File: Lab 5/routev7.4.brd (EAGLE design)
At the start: 100 x 80 mm, 48 parts, among them J2 FTDI_DEVICE, M1 WIRELESS-NRF24L01, U2 GY-521MPU6050, U3 ATMEGA328P_TQFP

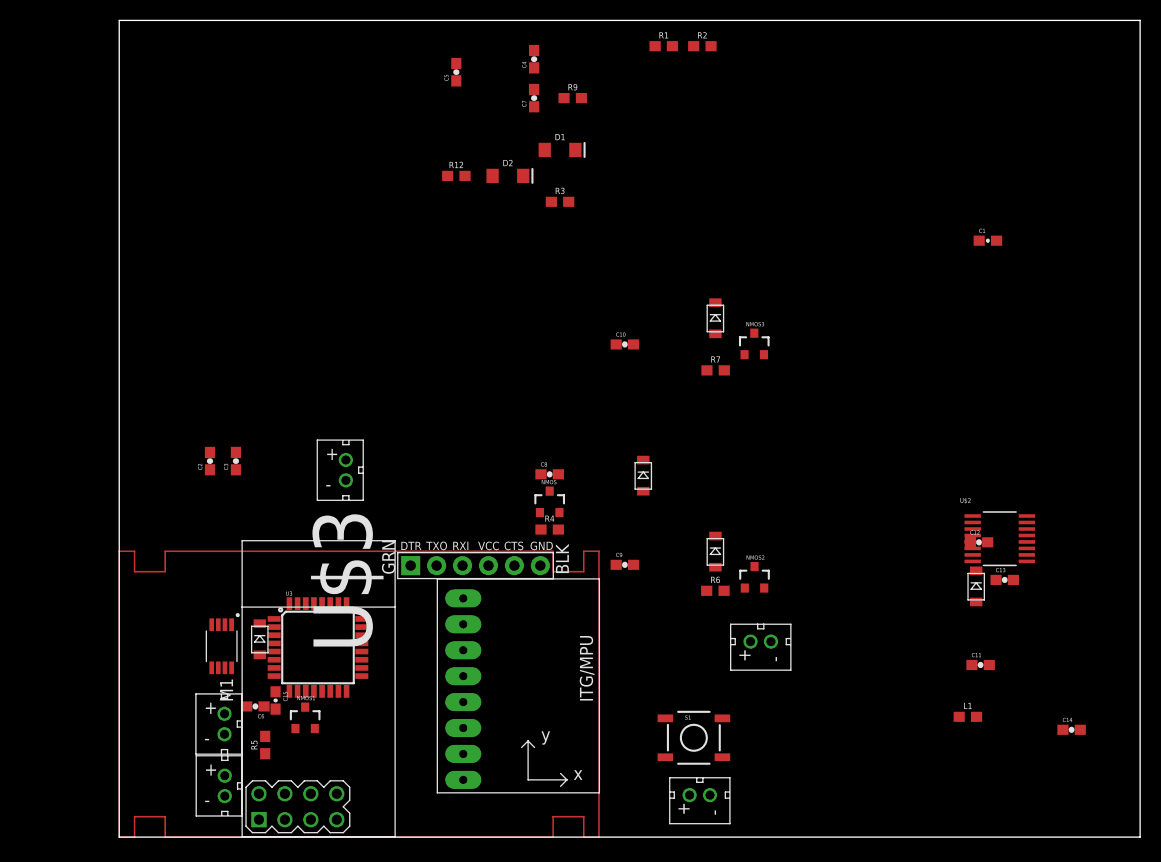
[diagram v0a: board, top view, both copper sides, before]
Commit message: Latest PCB at routev7.4.brd: no DRC error!!! Hurray!!!!!!
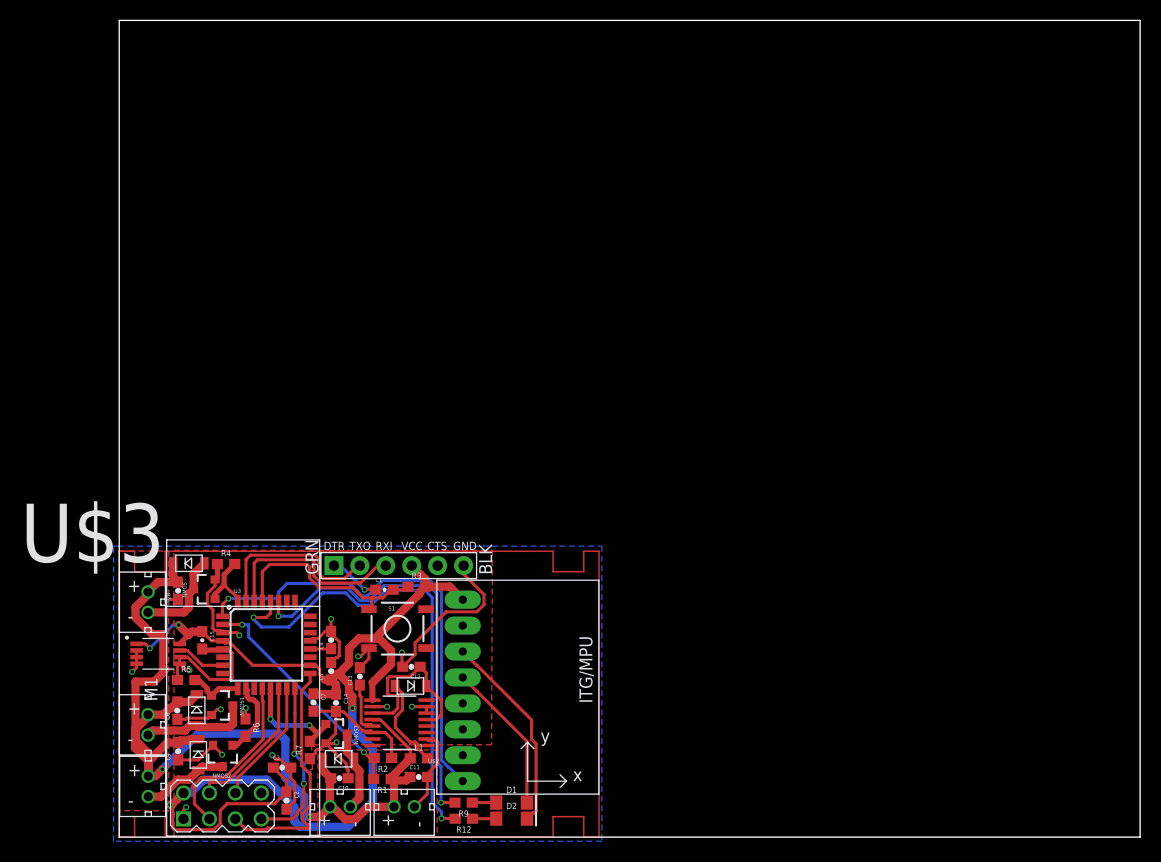
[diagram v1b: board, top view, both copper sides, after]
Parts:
- moved R1 76.9 mm to (25.8, 5.69), turned to 180 degrees
- moved R2 76.4 mm to (25.8, 7.75), turned to 180 degrees
- moved C14 72.1 mm to (21.2, 13.2), turned to 270 degrees
- moved R9 69.8 mm to (33.7, 3.38), turned to 180 degrees
- moved C1 68.3 mm to (26.0, 24.2)
- moved D1 64.1 mm to (38.4, 3.38)
- moved C13 63.9 mm to (23.6, 15.7), turned to 90 degrees
- moved C7 63.0 mm to (19.0, 13.2), turned to 270 degrees
- moved R12 63.0 mm to (33.8, 1.80), turned to 180 degrees
- moved D2 63.0 mm to (38.4, 1.80)
- moved U$2 61.5 mm to (27.5, 11.2), turned to 180 degrees
- moved C4 60.3 mm to (20.8, 19.3)
- moved MOTOR 60.1 mm to (2.82, 23.0), turned to 0 degrees
- moved C5 59.9 mm to (20.8, 16.3)
- moved C12 56.9 mm to (28.6, 16.7), turned to 180 degrees
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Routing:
- net VCC: track 0.00 -> 113.7 mm, vias 0 -> 4
- net GND: track 0.00 -> 111.9 mm, vias 0 -> 15
- net BATTERY+: track 0.00 -> 99.2 mm, vias 0 -> 2
- net N$10: track 0.00 -> 47.2 mm, vias 0 -> 2
- net IMU-INT: track 0.00 -> 45.0 mm, vias 0 -> 1
- net N$8: track 0.00 -> 41.6 mm, vias 0 -> 2
- net RF-SCK: track 0.00 -> 24.0 mm
- net MEASURE_PIN: track 0.00 -> 23.1 mm, vias 0 -> 2
- net RESET: track 0.00 -> 21.1 mm
- net IMU-SCL: track 0.00 -> 19.8 mm
- net FTDI-RX: track 0.00 -> 19.3 mm
- net FTDI-TX: track 0.00 -> 17.7 mm
- net RF-CE: track 0.00 -> 17.7 mm
- net VR-PS: track 0.00 -> 17.4 mm
- net RF-MISO: track 0.00 -> 16.7 mm, vias 0 -> 2
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- added copper zone on layer 1, net BATTERY_+
- added copper zone on layer 16, net GND
- added copper zone on layer 1, net S$1
- added copper zone on layer 1, net S$2
